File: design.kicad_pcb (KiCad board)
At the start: 4 copper layers, 65 x 36 mm, 30 parts, among them J1 Conn_01x03

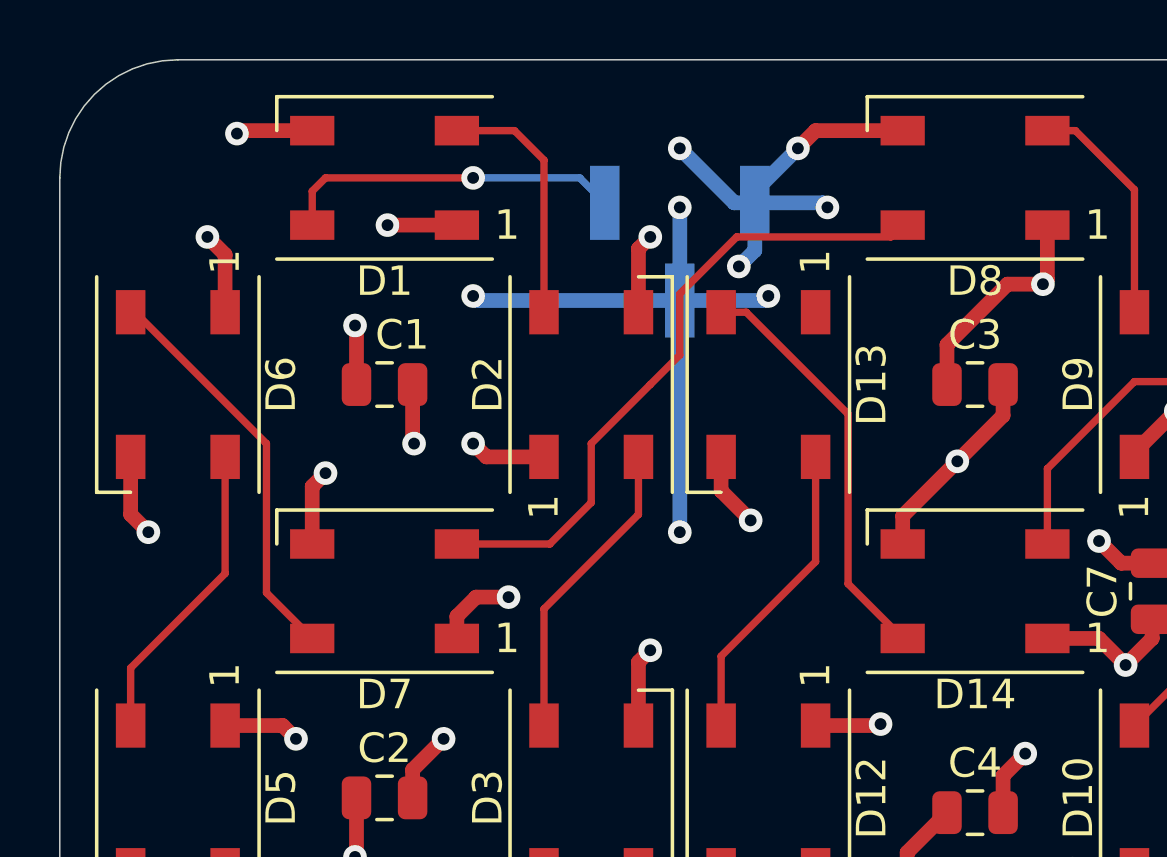
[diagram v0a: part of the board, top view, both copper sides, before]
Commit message: added big capacitor and resistor @input
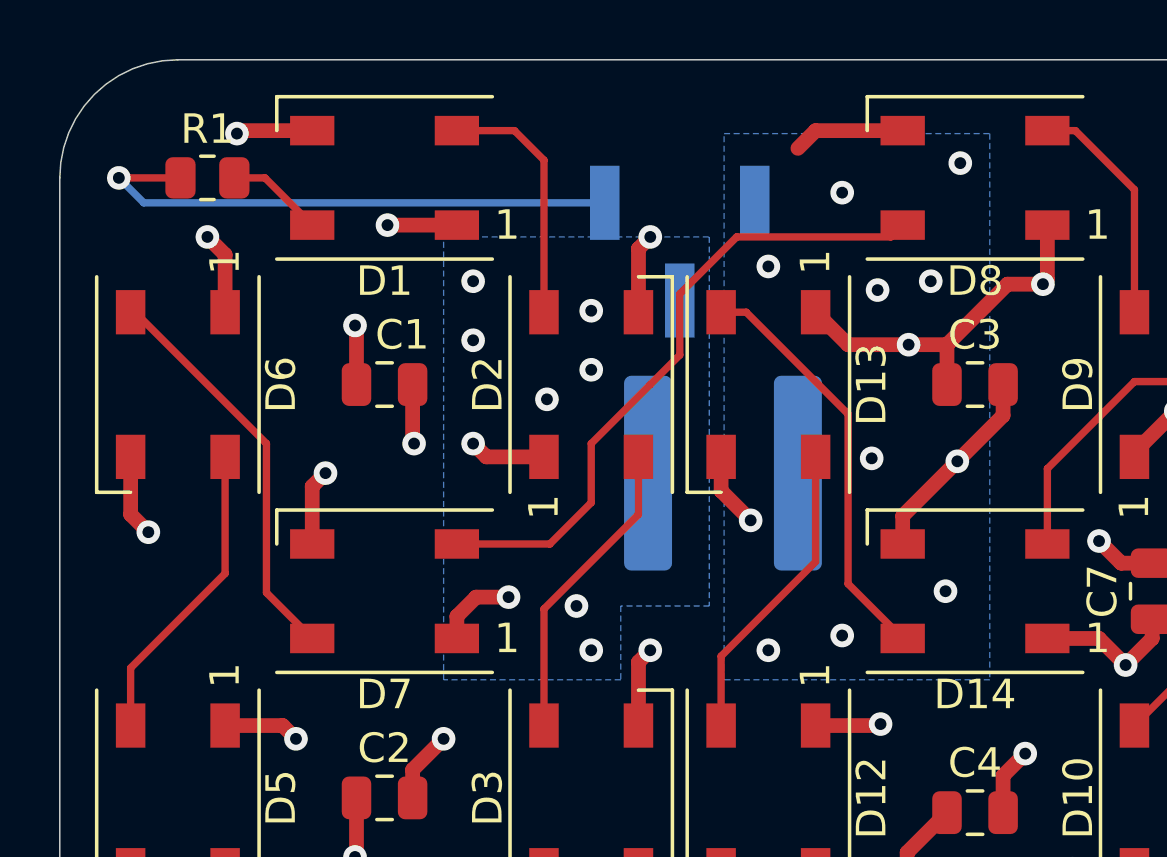
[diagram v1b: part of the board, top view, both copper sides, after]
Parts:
- added C8: 500-1000uF, Capacitor_SMD:C_2225_5664Metric, B.Cu at (108.5, 83.0)
- added R1: 500R, Resistor_SMD:R_0805_2012Metric, F.Cu at (91.0, 73.0)
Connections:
- J1 pad 1: Din -> Net-(J1-Pad1)
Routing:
- net Net-(J1-Pad1): track 0.00 -> 19.0 mm, vias 0 -> 1
- net VCC: track 94.3 -> 78.0 mm, vias 27 -> 31
- net GND: track 88.2 -> 77.9 mm, vias 29 -> 34
- net Din: track 11.7 -> 3.30 mm, vias 1 -> 0
- added copper zone on B.Cu, net GND
- added copper zone on B.Cu, net VCC

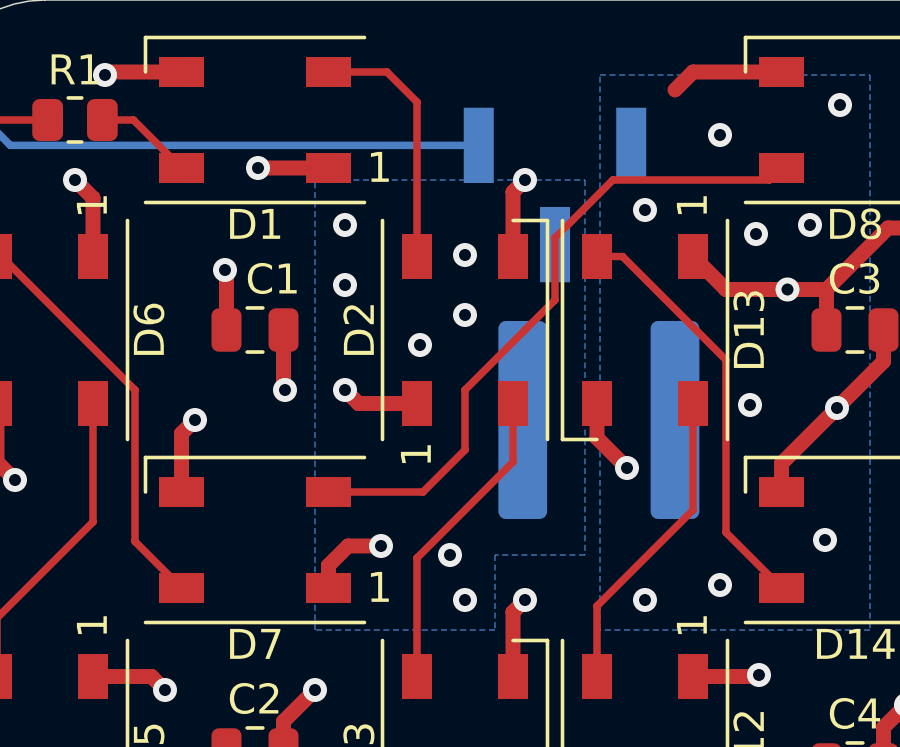
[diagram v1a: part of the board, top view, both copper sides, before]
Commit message: PCB: fix DRC error
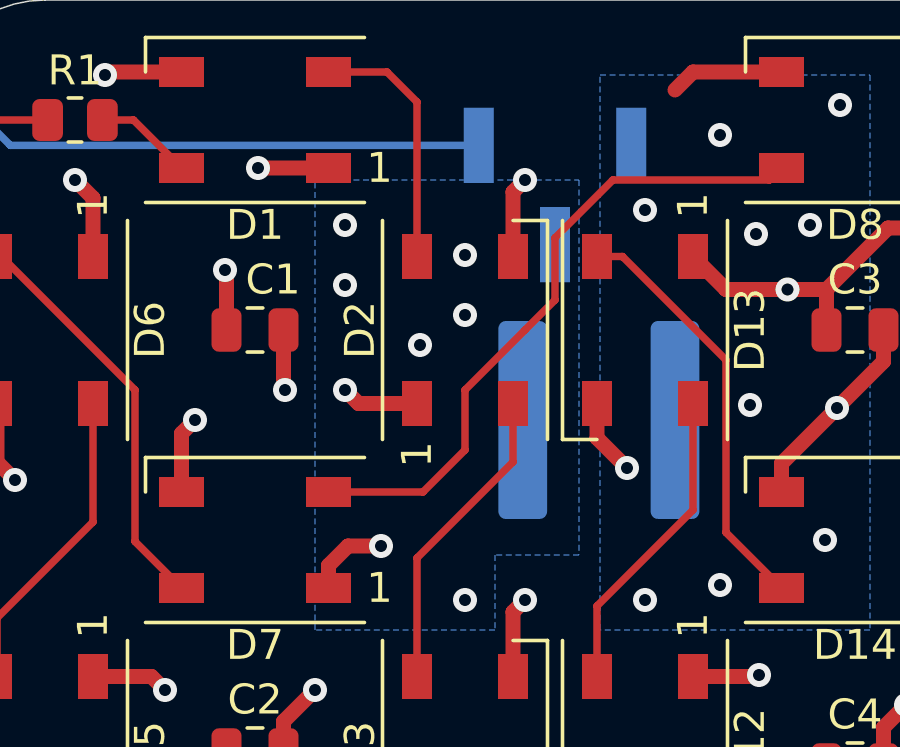
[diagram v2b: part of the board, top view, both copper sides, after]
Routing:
- net VCC: vias 31 -> 30
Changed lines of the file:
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@@
     (thickness 1.6)
     (drawings 42)
-    (tracks 264)
+    (tracks 263)
     (zones 0)
     (modules 32)
@@
   (layers
     (0 F.Cu signal)
-    (1 In1.Cu power)
-    (2 In2.Cu power)
+    (1 In1.Cu power hide)
+    (2 In2.Cu power hide)
     (31 B.Cu signal)
     (32 B.Adhes user)
@@
   (via (at 102.5 80.5) (size 0.8) (drill 0.4) (layers F.Cu B.Cu) (net 1))
   (via (at 104 89) (size 0.8) (drill 0.4) (layers F.Cu B.Cu) (net 1))
-  (via (at 103.5 87.5) (size 0.8) (drill 0.4) (layers F.Cu B.Cu) (net 1))
   (via (at 104 79.5) (size 0.8) (drill 0.4) (layers F.Cu B.Cu) (net 1))
   (segment (start 112.7 78.65) (end 114.75 78.65) (width 0.5) (layer F.Cu) (net 1))
@@
     (polygon
       (pts
-        (xy 108 87.5) (xy 105 87.5) (xy 105 90) (xy 99 90) (xy 99 75)
-        (xy 108 75)
+        (xy 107.8 87.5) (xy 105 87.5) (xy 105 90) (xy 99 90) (xy 99 75)
+        (xy 107.8 75)
       )
     )
